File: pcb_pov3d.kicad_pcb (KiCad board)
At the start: 4 copper layers, 98 x 69 mm, 93 parts, among them P1 CONN_4X2, P2 CONN_6, P3 MICRO-SD, P4 CONN_2, P5 KNUSB, P6 CONN_12, U1 TLC5955, U2 TLC5955, U3 TLC5955, U4 STM32F40X_LQFP64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

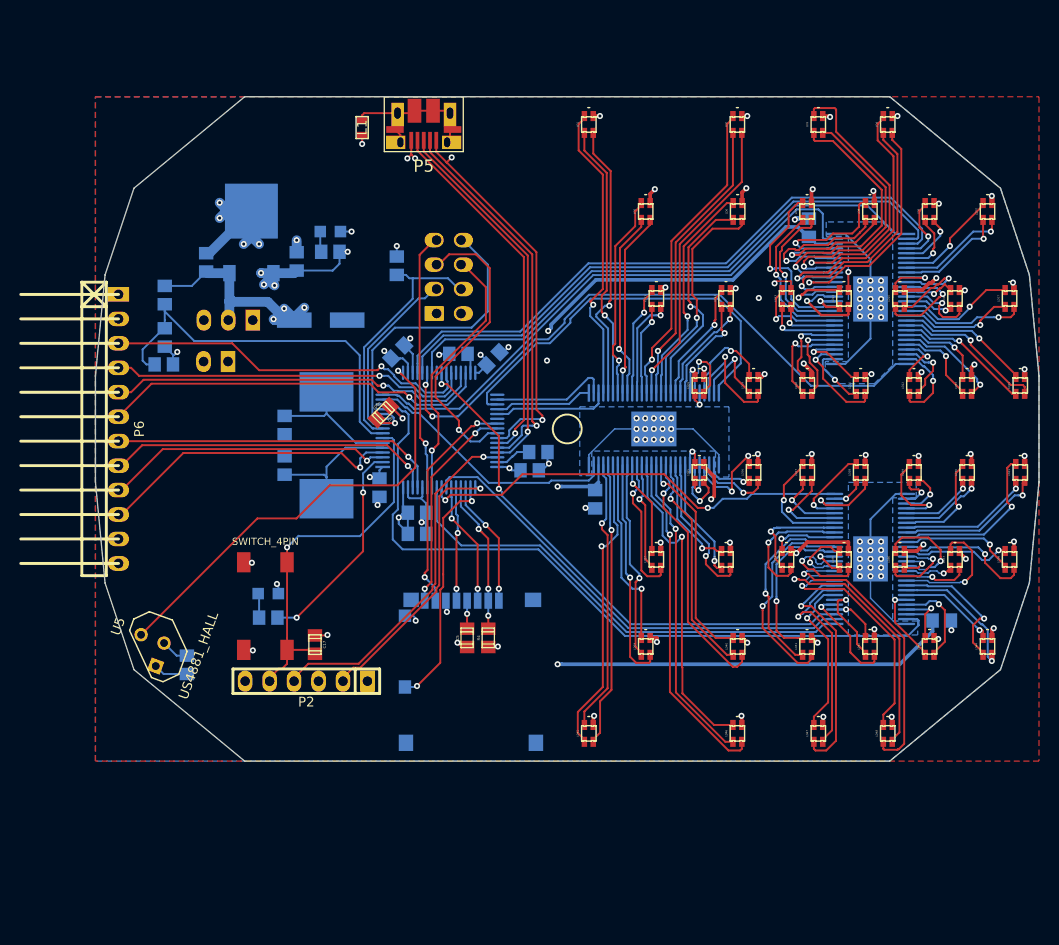
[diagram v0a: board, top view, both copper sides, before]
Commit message: Mounting holes - need some work, too close to LED.
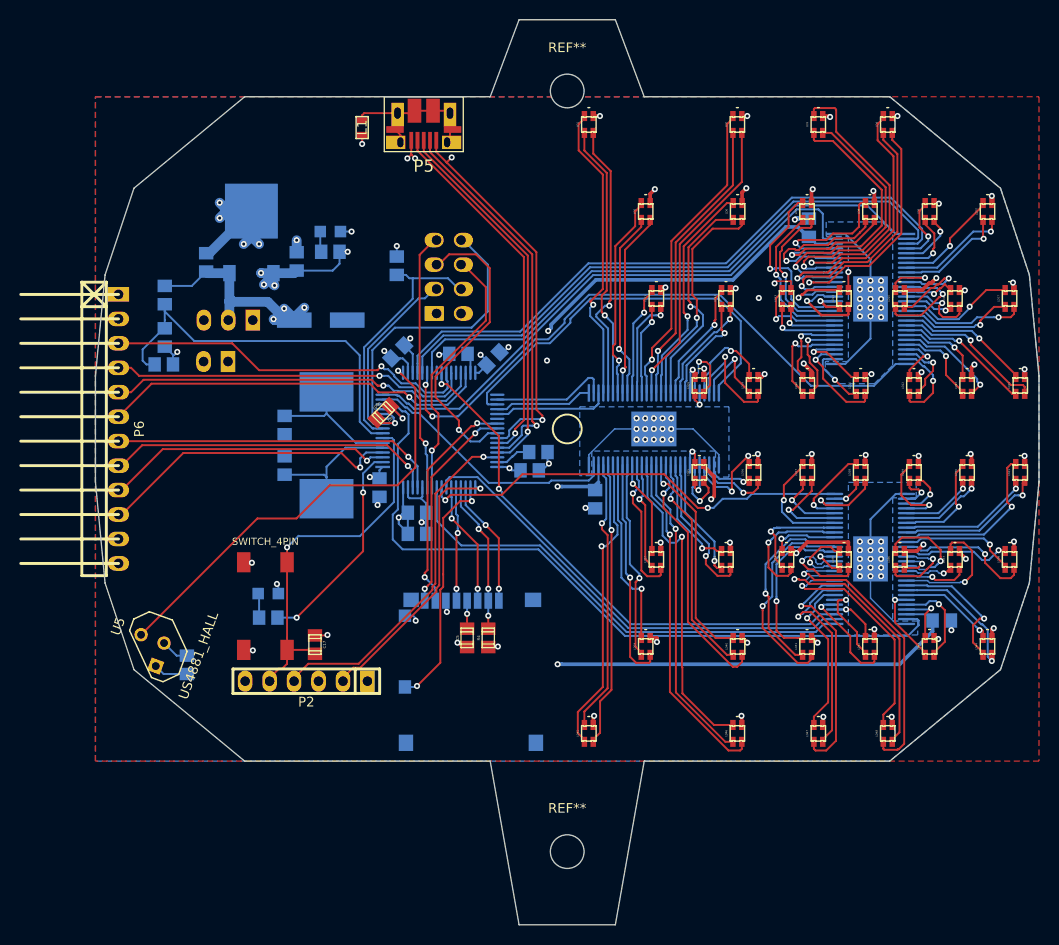
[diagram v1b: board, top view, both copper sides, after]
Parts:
- added REF**: MountingHole_3-5mm, Mounting_Holes:MountingHole_3-5mm, F.Cu at (100.0, 64.9)
- added REF**: MountingHole_3-5mm, Mounting_Holes:MountingHole_3-5mm, F.Cu at (100.0, 143.9)
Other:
- board size 98 x 69 mm -> 98 x 94 mm

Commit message: Improved mounting holes.
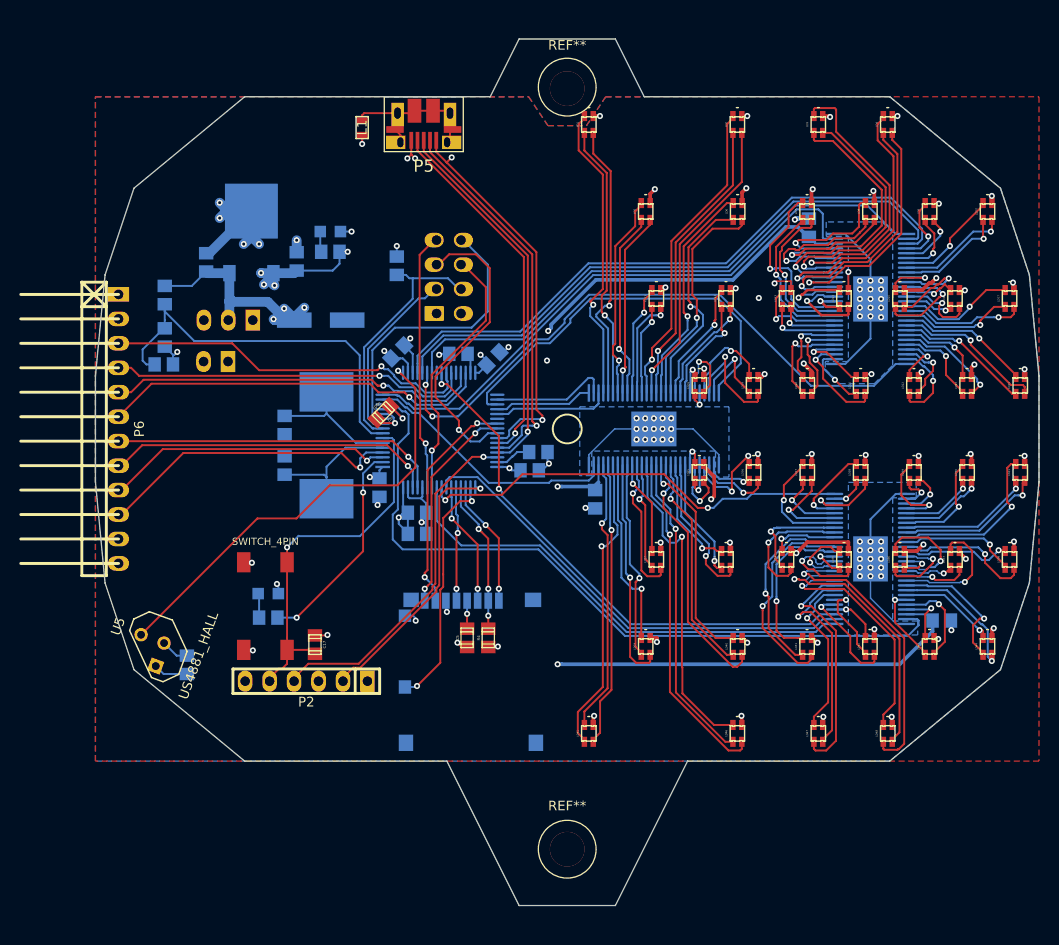
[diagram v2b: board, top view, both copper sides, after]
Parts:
- moved REF** 0.25 mm to (100.0, 64.7)
- moved REF** 0.25 mm to (100.0, 143.7)
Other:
- board size 98 x 94 mm -> 98 x 90 mm

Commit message: Move 2 TLCs 4mm to not conflict with spindle mount rim
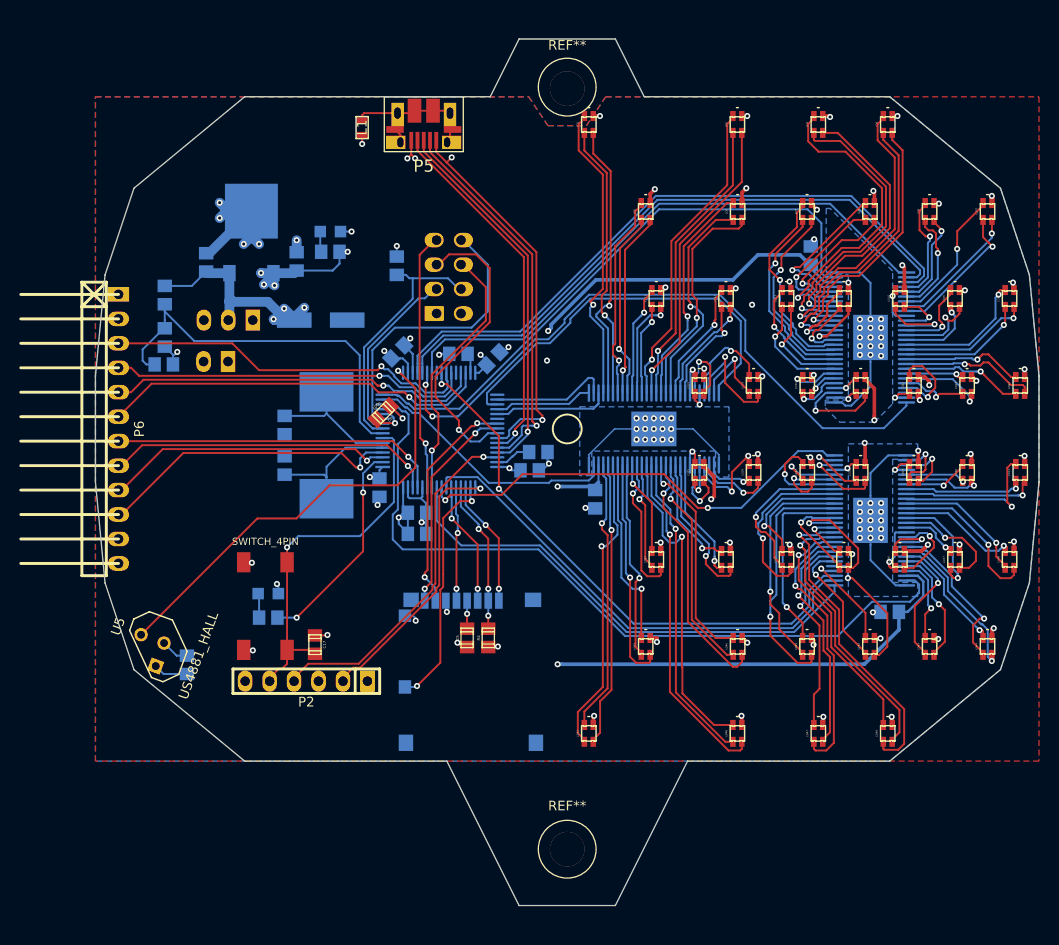
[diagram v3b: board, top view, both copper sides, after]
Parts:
- moved C3 5.47 mm to (133.5, 119.0), turned to 0 degrees
- moved U1 4.00 mm to (131.5, 90.5)
- moved U3 4.00 mm to (131.5, 109.5)
- moved C1 2.91 mm to (125.3, 82.0)
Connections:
- net +3.3V renamed +3V3
- U3 pad 42: /LEDs/led36g -> /LEDs/led37g
- U3 pad 43: /LEDs/led36r -> /LEDs/led37r
- U3 pad 44: /LEDs/led36b -> /LEDs/led37b
- U3 pad 45: /LEDs/led37g -> /LEDs/led36g
- U3 pad 46: /LEDs/led37r -> /LEDs/led36r
- U3 pad 47: /LEDs/led37b -> /LEDs/led36b
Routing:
- net +5V: track 513.1 -> 312.7 mm, vias 50 -> 51
- net GND: track 335.3 -> 250.8 mm, vias 74 -> 73
- net +3V3: track 293.8 -> 334.1 mm
- net /LEDs/led37b: track 13.4 -> 5.84 mm
- net /LEDs/led37g: track 5.23 -> 11.8 mm
- net /LEDs/led29b: track 9.43 -> 2.95 mm
- net /LEDs/led28b: track 8.87 -> 2.52 mm
- net /LEDs/led35g: track 3.94 -> 10.1 mm
- net /LEDs/led36b: track 11.5 -> 5.40 mm
- net /LEDs/led22g: track 8.90 -> 2.86 mm
- net /LEDs/led20r: track 9.03 -> 3.18 mm
- net /LEDs/led34b: track 7.04 -> 12.7 mm
- net /LEDs/led20g: track 10.1 -> 4.73 mm
- net /LEDs/led42b: track 5.28 -> 10.6 mm
- net /LEDs/led43g: track 8.21 -> 13.4 mm
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
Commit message: Misc. cleanup of the routing.
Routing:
- net +3V3: track 334.1 -> 170.7 mm
- net +5V: track 312.7 -> 153.1 mm
- net GND: track 250.8 -> 139.5 mm, vias 73 -> 74
- net /LEDs/sout2: track 42.2 -> 37.8 mm
- net /LEDs/sout1: track 68.5 -> 64.2 mm
- net /LEDs/led6g: track 23.2 -> 20.7 mm
- net /MCU_Pwr/osc_out: track 15.5 -> 13.8 mm
- net /LEDs/led6r: track 23.2 -> 21.7 mm
- net /LEDs/led1b: track 31.4 -> 30.1 mm
- net /LEDs/led1r: track 29.1 -> 27.9 mm
- net /LEDs/led12r: track 11.3 -> 12.1 mm
- net /LEDs/led6b: track 23.5 -> 22.8 mm
- net /LEDs/led11g: track 9.44 -> 10.1 mm
- net (no net): vias 1 -> 0

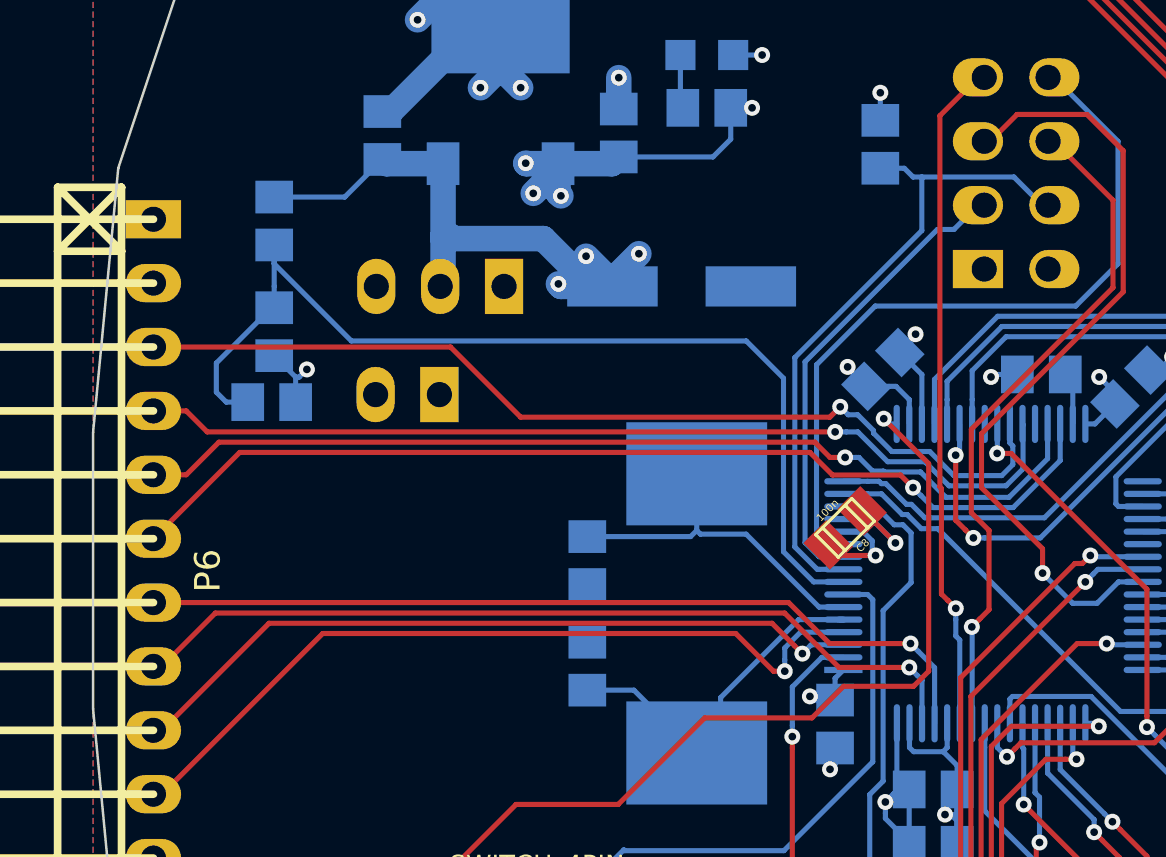
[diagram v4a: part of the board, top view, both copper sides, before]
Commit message: Move power connector and jumper away from rim of spindle_mount
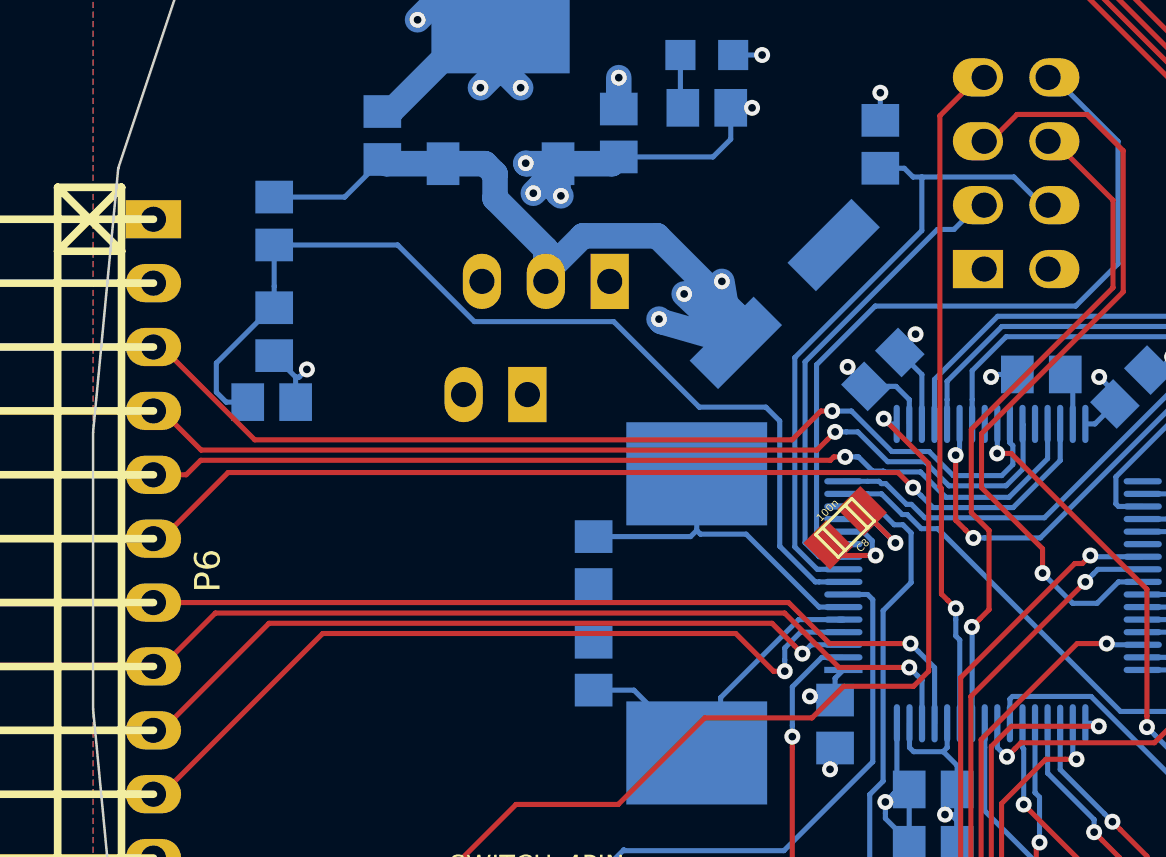
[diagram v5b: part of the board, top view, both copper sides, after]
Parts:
- moved JP1 4.20 mm to (69.0, 88.5)
- moved C20 4.11 mm to (78.5, 89.0), turned to 225 degrees
- moved P4 3.50 mm to (67.0, 93.0)
- moved C18 0.25 mm to (70.9, 103.8)
- moved C19 0.25 mm to (70.9, 99.6)
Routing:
- net +5V: track 153.1 -> 164.2 mm
- net /MCU_Pwr/vusb: track 83.1 -> 88.1 mm
- net /bat_sense: track 41.0 -> 39.5 mm
- net /pb0: track 38.5 -> 39.8 mm
- net /usart3_rx: track 40.6 -> 39.9 mm
- net /pb1: track 37.9 -> 38.5 mm
